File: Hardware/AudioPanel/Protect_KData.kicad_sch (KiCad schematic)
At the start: 34 parts

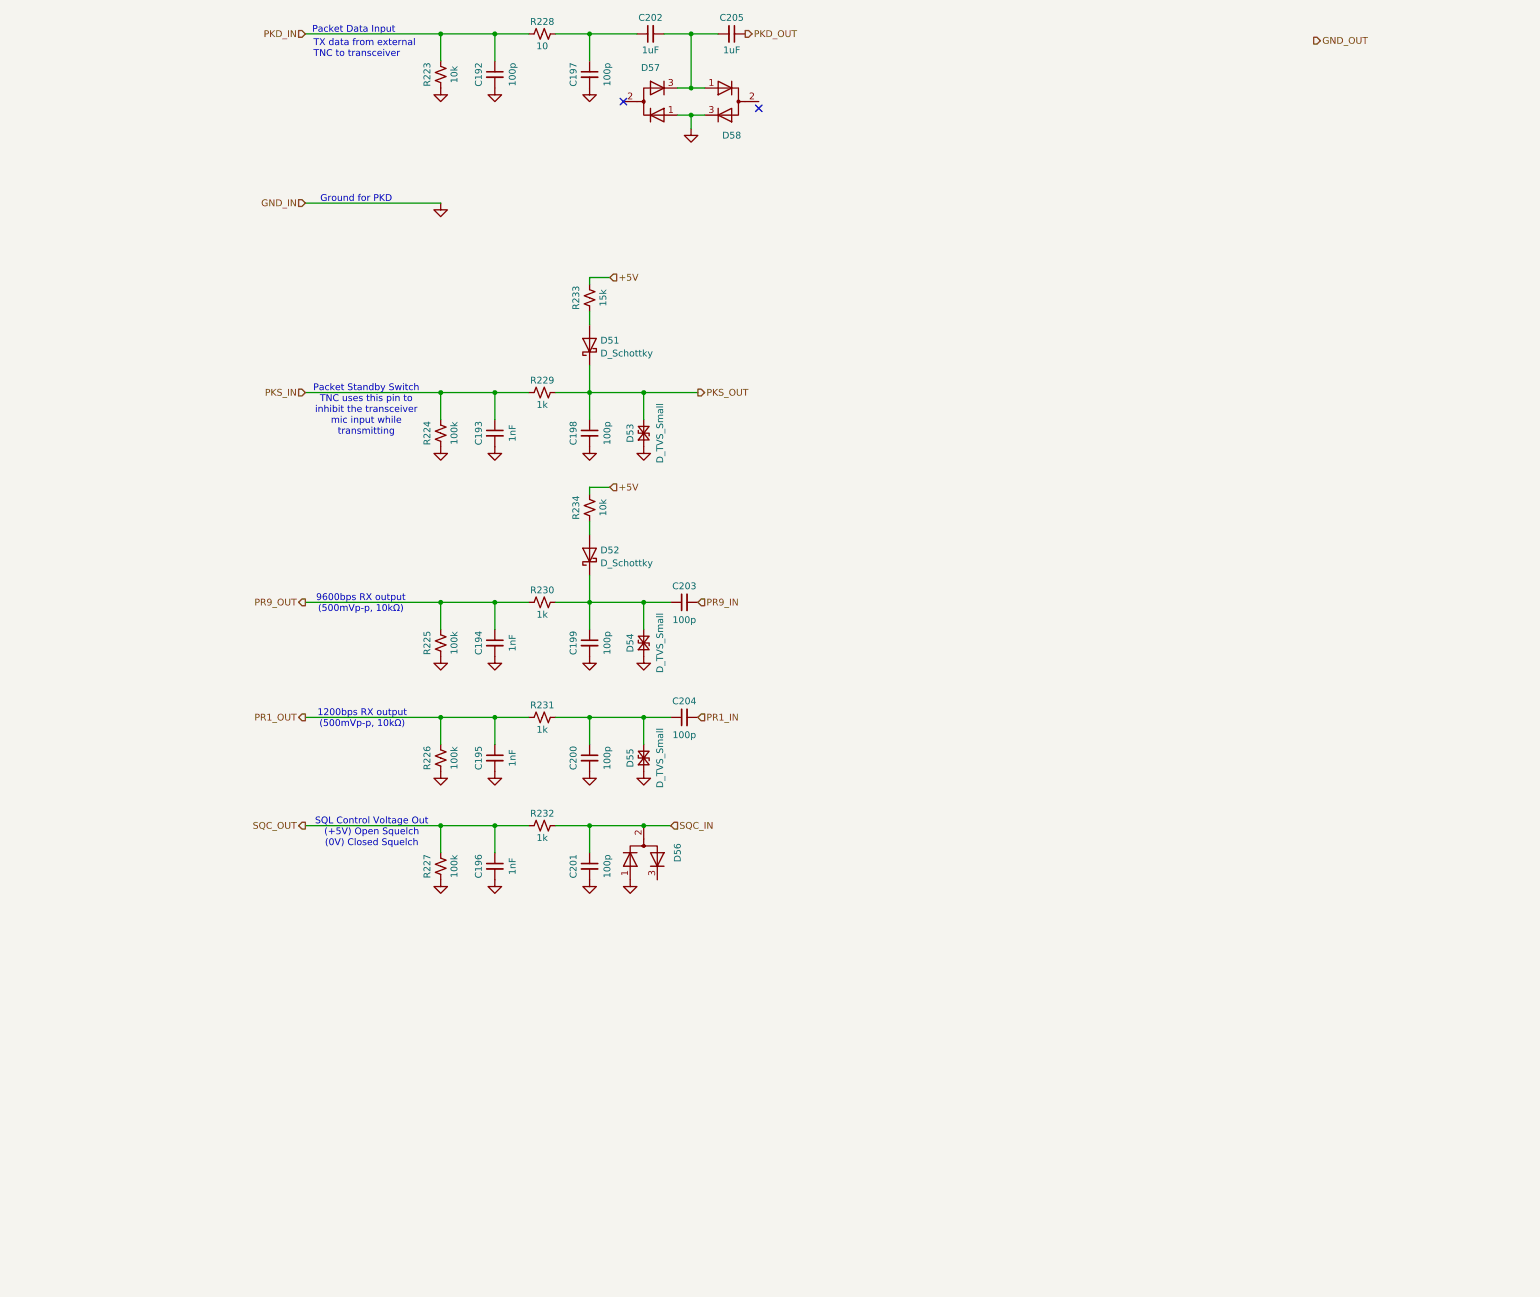
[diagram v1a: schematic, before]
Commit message: Added MIC port protections
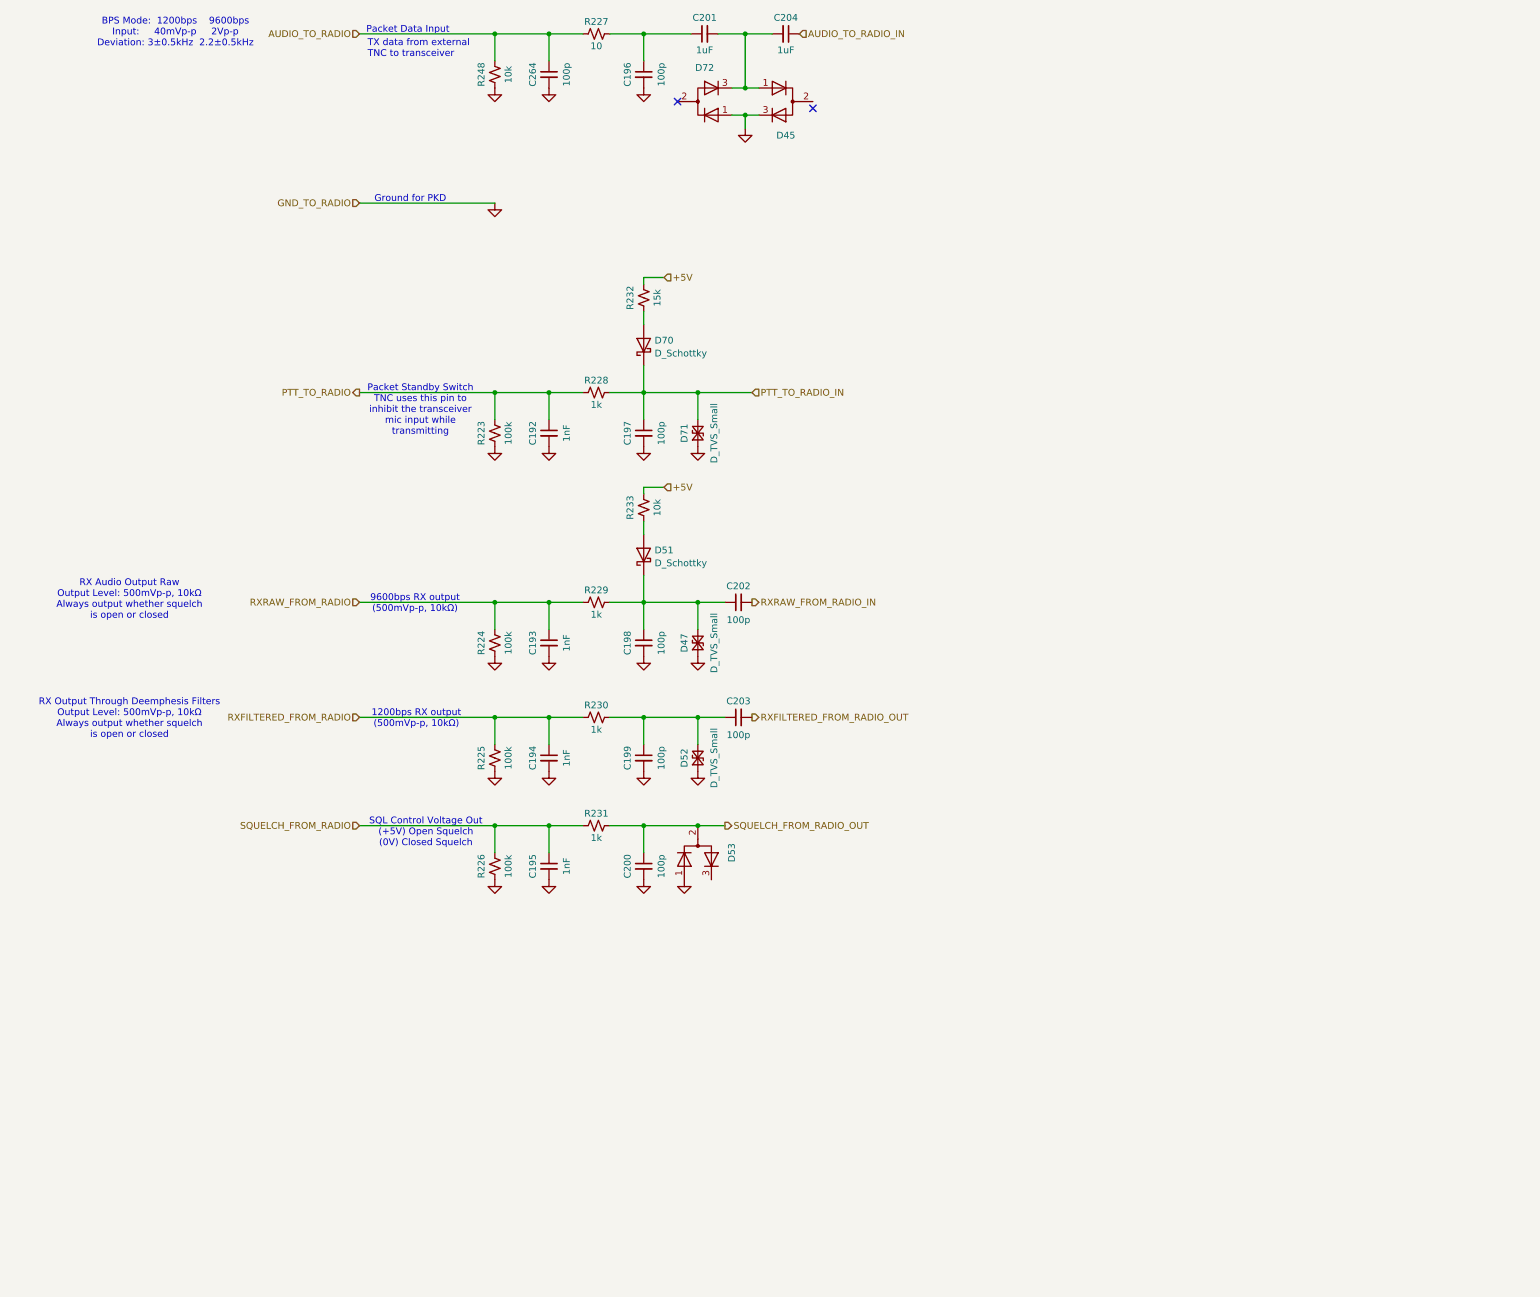
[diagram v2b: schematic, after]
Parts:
- renumbered C193 to C192, C194 to C193, C195 to C194, C196 to C195, C197 to C196, C198 to C197, C199 to C198, C200 to C199, C201 to C200, C202 to C201, C203 to C202, C204 to C203, C205 to C204, C192 to C264, D58 to D45, D54 to D47, D52 to D51, D55 to D52, D56 to D53, D51 to D70, D53 to D71, D57 to D72, R224 to R223, R225 to R224, R226 to R225, R227 to R226, R228 to R227, R229 to R228, R230 to R229, R231 to R230, R232 to R231, R233 to R232, R234 to R233, R223 to R248
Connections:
- net PKD_IN renamed AUDIO_TO_RADIO
- net PKD_OUT renamed AUDIO_TO_RADIO_IN
- net PKS_IN renamed PTT_TO_RADIO
- net PKS_OUT renamed PTT_TO_RADIO_IN
- net PR1_IN renamed RXFILTERED_FROM_RADIO_OUT
- net PR1_OUT renamed RXFILTERED_FROM_RADIO
- net PR9_IN renamed RXRAW_FROM_RADIO_IN
- net PR9_OUT renamed RXRAW_FROM_RADIO
- net SQC_IN renamed SQUELCH_FROM_RADIO_OUT
- net SQC_OUT renamed SQUELCH_FROM_RADIO
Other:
- note added: "BPS Mode: 1200bps 9600bps Input: 40mVp-p 2Vp-p Deviation: 3±0.5kHz 2.2±0.5kHz"
- note added: "RX Audio Output Raw Output Level: 500mVp-p, 10kΩ Always output whether squelch is open or closed"
- note added: "RX Output Through Deemphesis Filters Output Level: 500mVp-p, 10kΩ Always output whether squelch is open or closed"
- moved on the sheet: C192, C193, C194, C195, C196, C197, C198, C199, C200, C201, C202, C203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

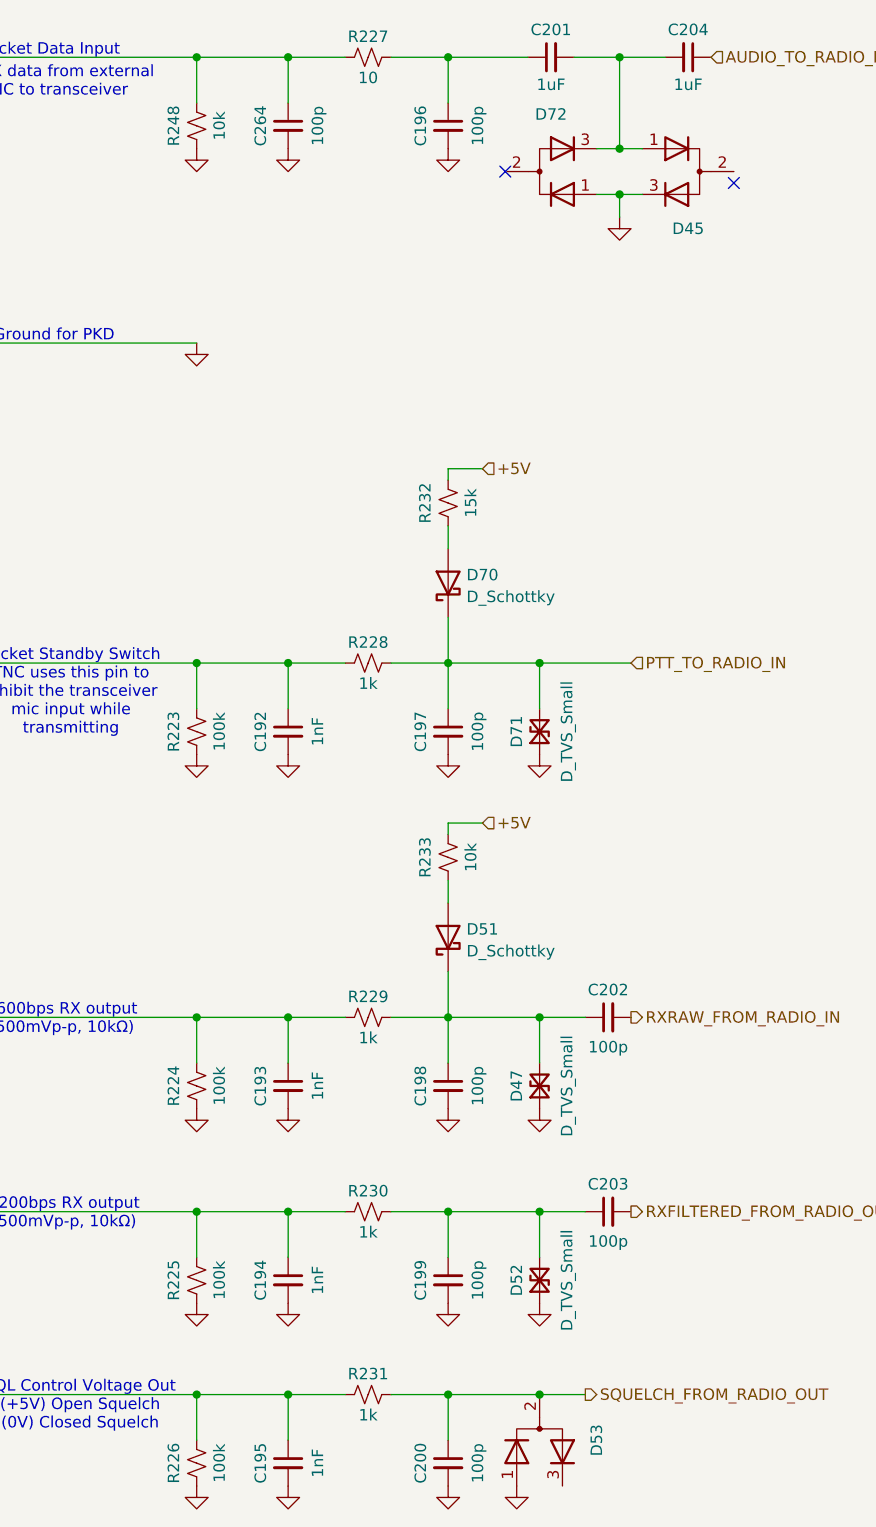
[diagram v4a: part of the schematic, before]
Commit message: Simplified COM switching, added USB-232
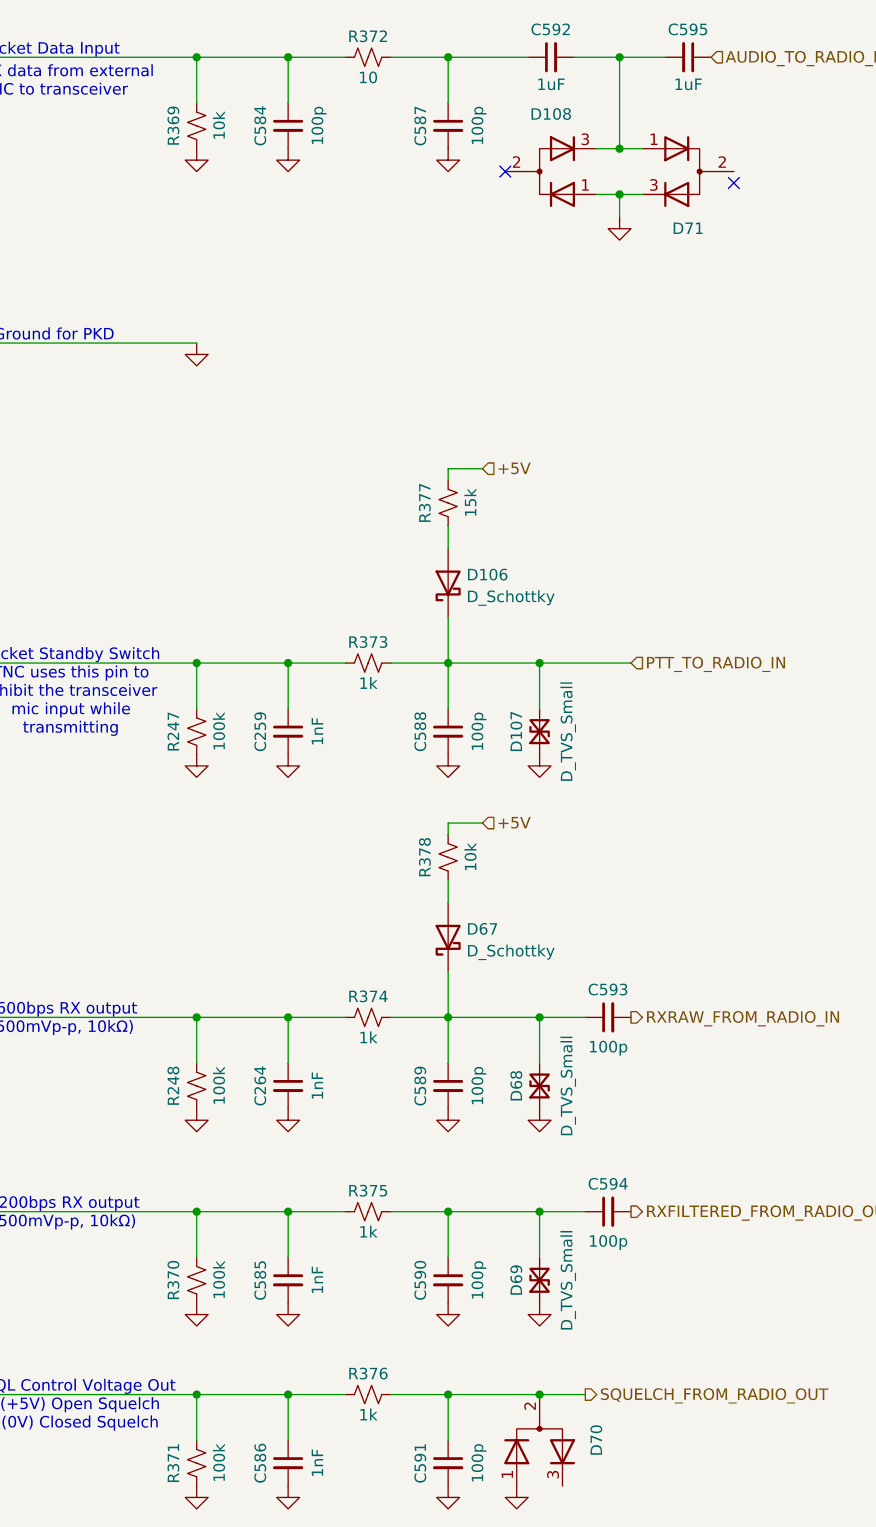
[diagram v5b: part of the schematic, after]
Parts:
- renumbered C192 to C259, C193 to C264, C264 to C584, C194 to C585, C195 to C586, C196 to C587, C197 to C588, C198 to C589, C199 to C590, C200 to C591, C201 to C592, C202 to C593, C203 to C594, C204 to C595, D70 to D106, D71 to D107, D72 to D108, D51 to D67, D47 to D68, D52 to D69, D53 to D70, D45 to D71, R223 to R247, R224 to R248, R248 to R369, R225 to R370, R226 to R371, R227 to R372, R228 to R373, R229 to R374, R230 to R375, R231 to R376, R232 to R377, R233 to R378
